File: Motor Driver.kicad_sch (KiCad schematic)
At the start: 18 parts, among them J501 Conn_01x02, J502 Conn_01x06, J503 Conn_01x06, Q2 AO3400A, U501 DRV8833PW

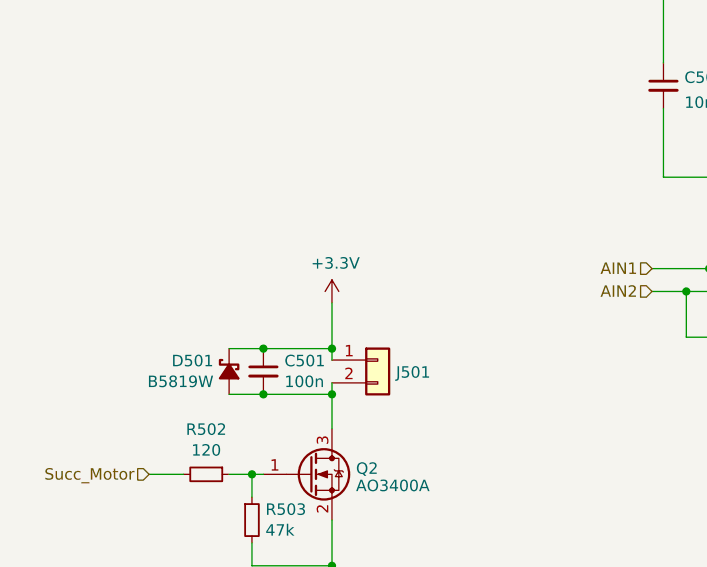
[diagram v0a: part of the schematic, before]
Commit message: improved sensor design
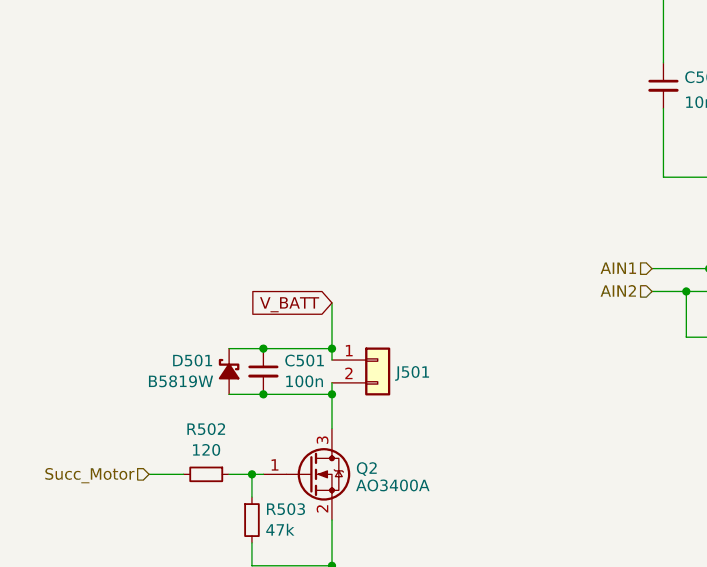
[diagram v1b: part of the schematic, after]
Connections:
- net +3V3: no longer C501.1, D501.1 (K), J501.1 (Pin_1)
- net V_BATT: now also C501.1, D501.1 (K), J501.1 (Pin_1)
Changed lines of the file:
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@@
+    )
+  )
+  (global_label "V_BATT" (shape input) (at 91.44 59.69 180) (fields_autoplaced)
+    (effects (font (size 1.27 1.27)) (justify right))
+    (property "Intersheetrefs" "${INTERSHEET_REFS}" (at 82.1842 59.69 0)
+      (effects (font (size 1.27 1.27)) (justify right) hide)
     )
   )
@@
     (effects (font (size 1.27 1.27)) (justify right))
   )
-  (symbol (lib_id "power:+3.3V") (at 91.44 59.69 0) (unit 1)
-    (in_bom yes) (on_board yes) (dnp no)
-    (property "Reference" "#PWR023" (at 91.44 63.5 0)
-      (effects (font (size 1.27 1.27)) hide)
-    )
-    (property "Value" "+3.3V" (at 91.821 55.2958 0)
-      (effects (font (size 1.27 1.27)))
-    )
-    (property "Footprint" "" (at 91.44 59.69 0)
-      (effects (font (size 1.27 1.27)) hide)
-    )
-    (property "Datasheet" "" (at 91.44 59.69 0)
-      (effects (font (size 1.27 1.27)) hide)
-    )
-    (pin "1")
-    (instances
-      (project "Line Tracer esp32"
-        (path "/281576c8-91a4-4828-9354-28c2f0a7e0e1/2542813a-b579-46cd-a0ba-c42901f79ac0"
-          (reference "#PWR023") (unit 1)
-        )
-      )
-      (project "Line Tracer"
-        (path "/2a1b4233-452a-404a-b933-88db3980ebb0/00000000-0000-0000-0000-000060ad1081"
-          (reference "#PWR076") (unit 1)
-        )
-      )
-      (project "Line Tracer F405RGT"
-        (path "/357df1bf-2fc8-4b26-bb86-5825f7b69aa9/00ff0f66-961d-4039-a1b9-9d9b8fb39bcb"
-          (reference "#PWR058") (unit 1)
-        )
-      )
-      (project "Line Tracer RP2040"
-        (path "/8c28d176-22ae-4483-9f62-5231c94718f1/d2751592-a077-484e-a0f8-daca799779d7"
-          (reference "#PWR0301") (unit 1)
-        )
-      )
-    )
-  )
   (symbol (lib_id "power:GND") (at 91.44 91.44 0) (unit 1)
